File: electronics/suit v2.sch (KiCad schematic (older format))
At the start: 3 parts

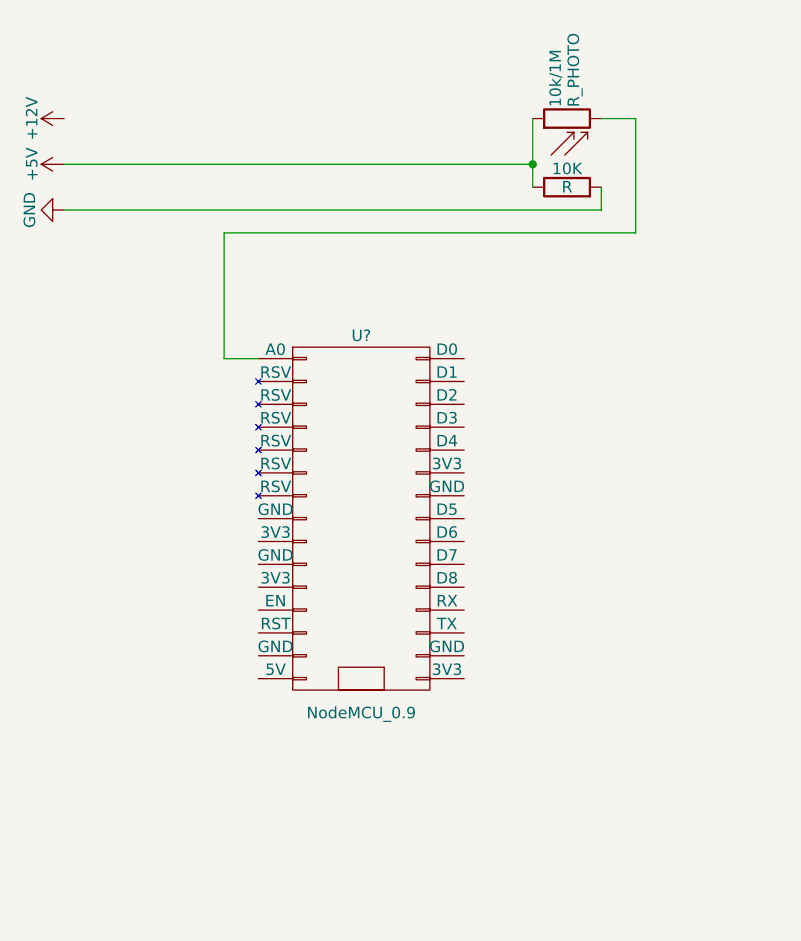
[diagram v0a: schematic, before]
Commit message: fix(schematics): update wiring diagrams
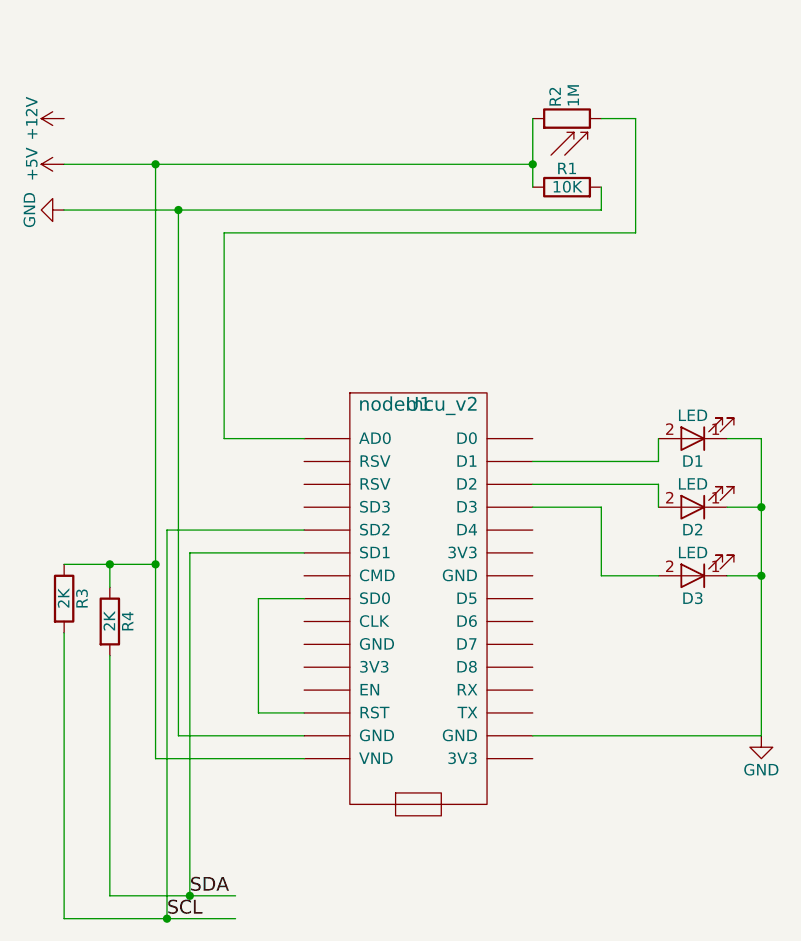
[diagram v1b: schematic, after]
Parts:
- removed U?: NodeMCU_0.9, symbol NodeMCU_0.9
- added D1, D2, D3: LED, symbol LED
- added R3, R4: 2K, symbol R
- added U1: nodemcu_v2, symbol nodemcu_v2
- R1: renamed from 10K; value R -> 10K
- R2: renamed from 10k/1M; value R_PHOTO -> 1M
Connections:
- net labels added: SCL, SDA
- wire segments 9 -> 38
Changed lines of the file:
@@
 LIBS:valves
 LIBS:nodemcu
+LIBS:nodemcu_v2
+LIBS:sensors
+LIBS:suit v2-cache
 EELAYER 25 0
 EELAYER END
@@
 $EndDescr
 $Comp
-L NodeMCU_0.9 U?
-U 1 1 59B44903
-P 2300 2800
-F 0 "U?" H 2300 3600 50  0000 C CNN
-F 1 "NodeMCU_0.9" H 2300 1950 50  0000 C CNN
-F 2 "" H 2550 2800 50  0000 C CNN
-F 3 "" H 2550 2800 50  0000 C CNN
-	1    2300 2800
-	1    0    0    -1
-$EndComp
-$Comp
-L +12V #PWR?
+L +12V #PWR01
 U 1 1 59B449AA
 P 1000 1050
-F 0 "#PWR?" H 1000 900 50  0001 C CNN
+F 0 "#PWR01" H 1000 900 50  0001 C CNN
 F 1 "+12V" H 1000 1190 50  0000 C CNN
 F 2 "" H 1000 1050 50  0001 C CNN
@@
 $EndComp
 $Comp
-L +5V #PWR?
+L +5V #PWR02
 U 1 1 59B449C2
 P 1000 1250
-F 0 "#PWR?" H 1000 1100 50  0001 C CNN
+F 0 "#PWR02" H 1000 1100 50  0001 C CNN
 F 1 "+5V" H 1000 1390 50  0000 C CNN
 F 2 "" H 1000 1250 50  0001 C CNN
@@
 $EndComp
 $Comp
-L GND #PWR?
+L GND #PWR03
 U 1 1 59B449D8
 P 1000 1450
-F 0 "#PWR?" H 1000 1200 50  0001 C CNN
+F 0 "#PWR03" H 1000 1200 50  0001 C CNN
 F 1 "GND" H 1000 1300 50  0000 C CNN
 F 2 "" H 1000 1450 50  0001 C CNN
@@
 $EndComp
 $Comp
-L R 10K
+L R R1
 U 1 1 59B44AEA
 P 3200 1350
-F 0 "10K" V 3280 1350 50  0000 C CNN
-F 1 "R" V 3200 1350 50  0000 C CNN
+F 0 "R1" V 3280 1350 50  0000 C CNN
+F 1 "10K" V 3200 1350 50  0000 C CNN
 F 2 "" V 3130 1350 50  0001 C CNN
 F 3 "" H 3200 1350 50  0001 C CNN
@@
 $EndComp
 $Comp
-L R_PHOTO 10k/1M
+L R_PHOTO R2
 U 1 1 59B44B19
 P 3200 1050
-F 0 "10k/1M" H 3250 1100 50  0000 L CNN
-F 1 "R_PHOTO" H 3250 1050 50  0000 L TNN
+F 0 "R2" H 3250 1100 50  0000 L CNN
+F 1 "1M" H 3250 1050 50  0000 L TNN
 F 2 "" V 3250 800 50  0001 L CNN
 F 3 "" H 3200 1000 50  0001 C CNN
@@
 	0    -1   -1   0
 $EndComp
+$Comp
+L nodemcu_v2 U1
+U 1 1 59B556D8
+P 2550 2300
+F 0 "U1" H 2550 2300 60  0000 C CNN
+F 1 "nodemcu_v2" H 2550 2300 60  0000 C CNN
+F 2 "" H 2550 2300 60  0001 C CNN
+F 3 "" H 2550 2300 60  0001 C CNN
+	1    2550 2300
+	1    0    0    -1
+$EndComp
+$Comp
+L LED D1
+U 1 1 59B558B4
+P 3750 2450
+F 0 "D1" H 3750 2550 50  0000 C CNN
+F 1 "LED" H 3750 2350 50  0000 C CNN
+F 2 "" H 3750 2450 50  0001 C CNN
+F 3 "" H 3750 2450 50  0001 C CNN
+	1    3750 2450
+	-1   0    0    1
+$EndComp
+$Comp
+L LED D2
+U 1 1 59B558D5
+P 3750 2750
+F 0 "D2" H 3750 2850 50  0000 C CNN
+F 1 "LED" H 3750 2650 50  0000 C CNN
+F 2 "" H 3750 2750 50  0001 C CNN
+F 3 "" H 3750 2750 50  0001 C CNN
+	1    3750 2750
+	-1   0    0    1
+$EndComp
+$Comp
+L LED D3
+U 1 1 59B558FC
+P 3750 3050
+F 0 "D3" H 3750 3150 50  0000 C CNN
+F 1 "LED" H 3750 2950 50  0000 C CNN
+F 2 "" H 3750 3050 50  0001 C CNN
+F 3 "" H 3750 3050 50  0001 C CNN
+	1    3750 3050
+	-1   0    0    1
+$EndComp
+$Comp
+L GND #PWR04
+U 1 1 59B55A07
+P 4050 3750
+F 0 "#PWR04" H 4050 3500 50  0001 C CNN
+F 1 "GND" H 4050 3600 50  0000 C CNN
+F 2 "" H 4050 3750 50  0001 C CNN
+F 3 "" H 4050 3750 50  0001 C CNN
+	1    4050 3750
+	1    0    0    -1
+$EndComp
+Text Label 1450 4550 0    60   ~ 0
+SCL
+Text Label 1550 4450 0    60   ~ 0
+SDA
+$Comp
+L R R4
+U 1 1 59B55F41
+P 1200 3250
+F 0 "R4" V 1280 3250 50  0000 C CNN
+F 1 "2K" V 1200 3250 50  0000 C CNN
+F 2 "" V 1130 3250 50  0001 C CNN
+F 3 "" H 1200 3250 50  0001 C CNN
+	1    1200 3250
+	1    0    0    -1
+$EndComp
+$Comp
+L R R3
+U 1 1 59B55FEA
+P 1000 3150
+F 0 "R3" V 1080 3150 50  0000 C CNN
+F 1 "2K" V 1000 3150 50  0000 C CNN
+F 2 "" V 930 3150 50  0001 C CNN
+F 3 "" H 1000 3150 50  0001 C CNN
+	1    1000 3150
+	1    0    0    -1
+$EndComp
 Wire Wire Line
 	1000 1250 3050 1250
@@
 	3500 1550 1700 1550
 Wire Wire Line
-	1700 1550 1700 2100
-Wire Wire Line
-	1700 2100 1850 2100
+	1700 1550 1700 2450
+Wire Wire Line
+	1700 2450 2050 2450
+Wire Wire Line
+	1400 1250 1400 3850
+Wire Wire Line
+	1400 3850 2050 3850
+Connection ~ 1400 1250
+Wire Wire Line
+	3050 2550 3600 2550
+Wire Wire Line
+	3600 2550 3600 2450
+Wire Wire Line
+	3050 2650 3600 2650
+Wire Wire Line
+	3600 2650 3600 2750
+Wire Wire Line
+	3050 2750 3350 2750
+Wire Wire Line
+	3350 2750 3350 3050
+Wire Wire Line
+	3350 3050 3600 3050
+Wire Wire Line
+	4050 2450 4050 3750
+Wire Wire Line
+	4050 3750 3050 3750
+Wire Wire Line
+	1850 3150 1850 3650
+Wire Wire Line
+	1850 3650 2050 3650
+Wire Wire Line
+	2050 2950 1550 2950
+Wire Wire Line
+	1550 2950 1550 4450
+Wire Wire Line
+	1200 4450 1750 4450
+Wire Wire Line
+	2050 2850 1450 2850
+Wire Wire Line
+	1450 2850 1450 4550
+Wire Wire Line
+	1000 4550 1750 4550
+Wire Wire Line
+	1400 3000 1000 3000
+Connection ~ 1400 3000
+Wire Wire Line
+	1200 3400 1200 4450
+Connection ~ 1550 4450
+Wire Wire Line
+	1000 3300 1000 4550
+Connection ~ 1450 4550
+Wire Wire Line
+	3900 2450 4050 2450
+Wire Wire Line
+	3900 2750 4050 2750
+Connection ~ 4050 2750
+Wire Wire Line
+	3900 3050 4050 3050
+Connection ~ 4050 3050
+Wire Wire Line
+	2050 3150 1850 3150
+Wire Wire Line
+	1200 3100 1200 3000
+Connection ~ 1200 3000
+Wire Wire Line
+	1500 1450 1500 3750
+Wire Wire Line
+	1500 3750 2050 3750
+Connection ~ 1500 1450
 $EndSCHEMATC
